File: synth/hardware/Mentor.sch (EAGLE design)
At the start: 36 parts, among them IC1 MCP23017SO

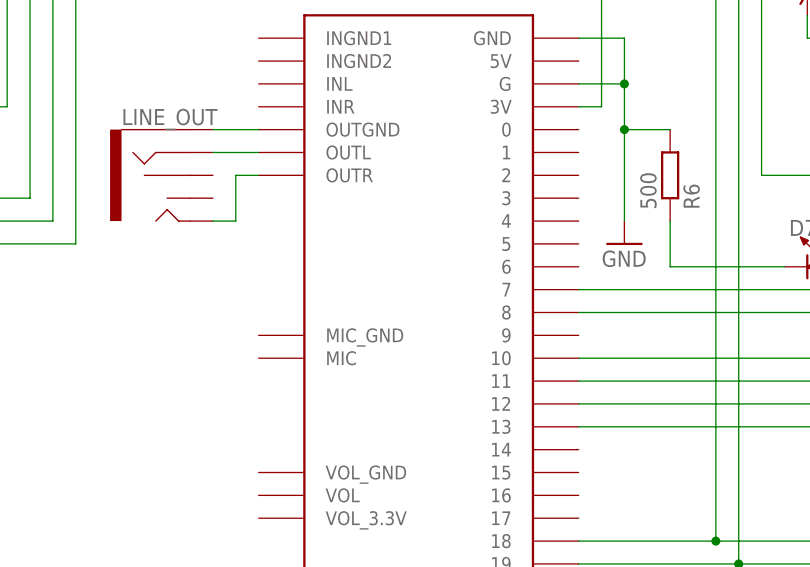
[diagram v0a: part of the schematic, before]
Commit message: Update - tests and wavefolding
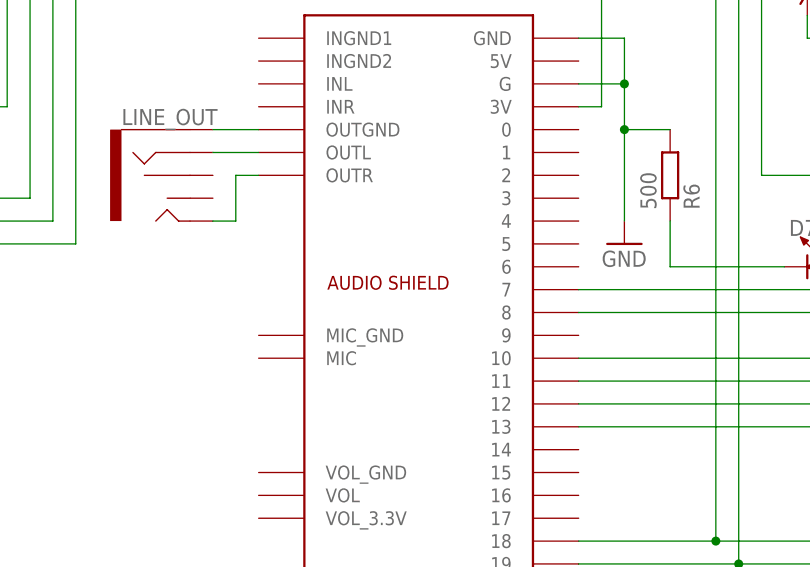
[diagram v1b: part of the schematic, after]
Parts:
- U$3: value (none) -> AUDIO SHIELD
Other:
- note added: "AUDIO SHIELD"
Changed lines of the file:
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@@
 <?xml version="1.0" encoding="utf-8"?>
 <!DOCTYPE eagle SYSTEM "eagle.dtd">
-<eagle version="7.3.0">
+<eagle version="8.2.1">
 <drawing>
 <settings>
@@
 <part name="SUPPLY4" library="supply2" deviceset="VCC" device=""/>
 <part name="GND7" library="supply1" deviceset="GND" device=""/>
-<part name="U$3" library="Teensy_Audioshield_alt" deviceset="AUDIOSHIELD" device=""/>
+<part name="U$3" library="Teensy_Audioshield_alt" deviceset="AUDIOSHIELD" device="" value="AUDIO SHIELD"/>
 <part name="IC1" library="adafruit" deviceset="MCP23017" device="SO" value="MCP23017SO"/>
 <part name="GND1" library="supply1" deviceset="GND" device=""/>
@@
 <sheet>
 <plain>
+<text x="53.34" y="60.96" size="1.524" layer="94">AUDIO SHIELD</text>
 </plain>
 <instances>
